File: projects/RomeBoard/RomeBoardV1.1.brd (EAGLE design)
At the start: 120 x 140 mm, 31 parts, among them J1 HEADER-5, J2 RASPBERRY-PI-HEADER, M1 ZVN4424A, M2 ZVN4424A, M3 ZVN4424A, U1 LM1084IT-ADJ

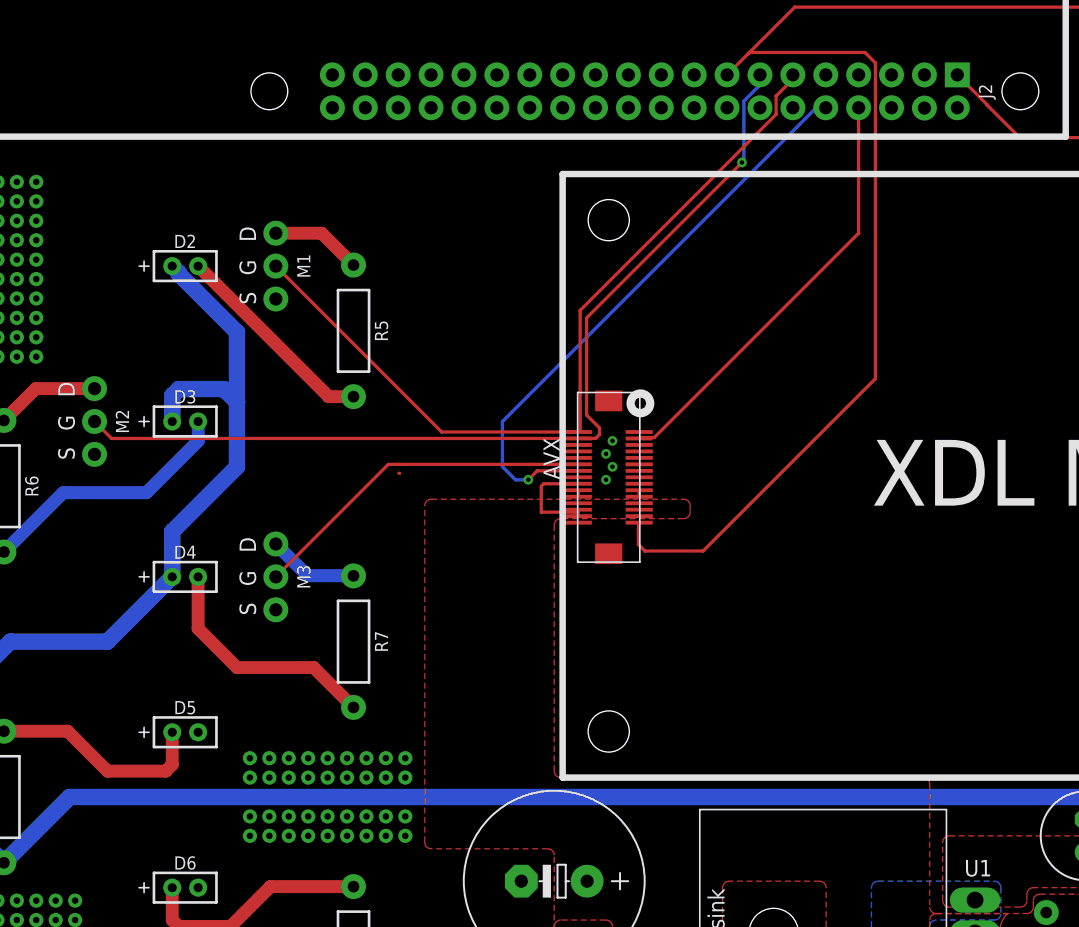
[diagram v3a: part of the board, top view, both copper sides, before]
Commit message: Adding gate pulldowns for NPNs
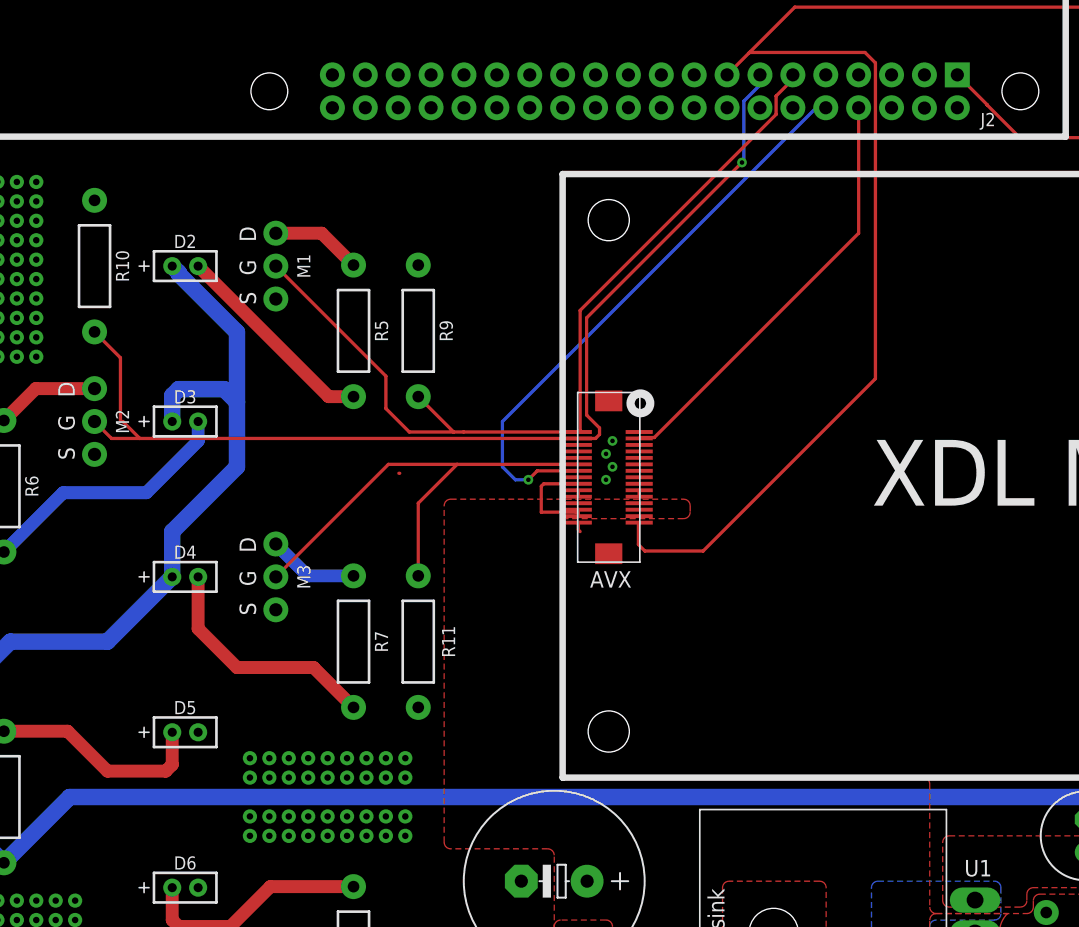
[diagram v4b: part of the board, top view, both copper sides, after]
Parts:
- added R10, R11, R9: 10K, passives:AXIAL-0.4
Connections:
- net GND: now also R10.1, R11.1, R9.1
- net PWR_L: now also R11.2
- net RX_L: now also R10.2
- net TX_L: now also R9.2
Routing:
- net PWR_L: track 27.0 -> 36.8 mm
- net RX_L: track 73.4 -> 83.2 mm
- net TX_L: track 63.1 -> 68.4 mm
- net GND: track 1.07 -> 1.82 mm
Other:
- board text added: "XDL Micro: 435.55MHz"
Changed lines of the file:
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@@
 <hole x="5" y="135" drill="2.844"/>
 <hole x="115" y="135" drill="2.844"/>
-<text x="16" y="133.5" size="3.2" layer="51" font="vector" ratio="19">BROWN SPACE ENGINEERING GROUND STATION</text>
+<text x="17" y="134" size="3.2" layer="51" font="vector" ratio="19">BROWN SPACE ENGINEERING GROUND STATION</text>
 <text x="99.5" y="130.5" size="1.27" layer="51" font="vector" ratio="13">Pi Power</text>
 <text x="106.5" y="103.5" size="2" layer="51" font="vector" ratio="13" align="center">Brown U.
@@
 <text x="16.5" y="11.5" size="1.6764" layer="51" font="vector" ratio="13">3.6V</text>
 <text x="17.5" y="23.5" size="1.6764" layer="51" font="vector" ratio="13">5V</text>
-<text x="107" y="79" size="2.5" layer="51" font="vector" ratio="13" rot="R30" align="center">Che piacere
+<text x="107" y="77.5" size="2.5" layer="51" font="vector" ratio="13" rot="R30" align="center">Che piacere
 vederti!</text>
 <circle x="115" y="135" radius="3.7" width="0.254" layer="20"/>
@@
 <rectangle x1="94.639690625" y1="125.46175" x2="94.784465625" y2="125.51000625" layer="51"/>
 <rectangle x1="94.398390625" y1="125.510009375" x2="94.687946875" y2="125.558265625" layer="51"/>
+<text x="47" y="24" size="1.4224" layer="51" font="vector" ratio="13" rot="R90">XDL Micro: 435.55MHz</text>
 </plain>
 <attributes>
@@
 </autorouter>
 <elements>
-<element name="AVX" library="CNTRL_BOARD" package="AVX-24-5046-630-829" value="AVX-24-5046-030-630-829" x="51.71" y="46.74" rot="R270"/>
+<element name="AVX" library="CNTRL_BOARD" package="AVX-24-5046-630-829" value="AVX-24-5046-030-630-829" x="51.71" y="46.74" smashed="yes" rot="R270">
+<attribute name="NAME" x="50.26" y="38.17" size="1.27" layer="21"/>
+</element>
 <element name="V4" library="BrownSpaceEngineering" package="VIA-120MIL" value="GND" x="14.25" y="4.94" smashed="yes">
 <attribute name="VALUE" x="16.21" y="6.98" size="1.016" layer="27" font="vector" ratio="13"/>
@@
 </element>
 <element name="U$2" library="BrownSpaceEngineering" package="PJ-002A" value="PJ-002A" x="110" y="11" rot="R270"/>
-<element name="J2" library="BrownSpaceEngineering" package="HEADER-20X02" value="RASPBERRY-PI-HEADER" x="54.5" y="76.5" rot="R270"/>
+<element name="J2" library="BrownSpaceEngineering" package="HEADER-20X02" value="RASPBERRY-PI-HEADER" x="54.5" y="76.5" smashed="yes" rot="R270">
+<attribute name="NAME" x="81" y="73.8064" size="1.016" layer="25" font="vector" ratio="20" align="bottom-center"/>
+</element>
 <element name="J1" library="BrownSpaceEngineering" package="HEADER-05" value="HEADER-5" x="103" y="128.5" rot="R180"/>
 <element name="D2" library="BrownSpaceEngineering" package="1X2-POL" value="LEDTHRU-HOLE-CONNECTOR" x="19" y="63" smashed="yes">
@@
 <attribute name="VALUE" x="95.429" y="89.794" size="1.27" layer="27" ratio="10" rot="R180"/>
 </element>
+<element name="R9" library="passives" package="AXIAL-0.4" value="10K" x="37" y="58" rot="R270"/>
+<element name="R10" library="passives" package="AXIAL-0.4" value="10K" x="12" y="63" rot="R270"/>
+<element name="R11" library="passives" package="AXIAL-0.4" value="10K" x="37" y="34" smashed="yes" rot="R90">
+<attribute name="NAME" x="39.849" y="34" size="1.016" layer="25" font="vector" ratio="20" rot="R90" align="bottom-center"/>
+<attribute name="VALUE" x="37.508" y="34" size="1.016" layer="27" font="vector" ratio="20" rot="R90" align="bottom-center"/>
+</element>
 </elements>
 <signals>
@@
 <contactref element="C1" pad="-"/>
 <contactref element="C3" pad="-"/>
-<wire x1="49.36" y1="45.69" x2="49.36" y2="45.19" width="0.254" layer="1"/>
 <via x="52" y="49.5" extent="1-16" drill="0.35"/>
 <via x="51.5" y="48.5" extent="1-16" drill="0.35"/>
@@
 <contactref element="C5" pad="2"/>
 <contactref element="FAN2" pad="2"/>
-<wire x1="49.36" y1="45.19" x2="49.36" y2="43.19" width="0" layer="19" extent="1-1"/>
+<wire x1="49.36" y1="45.19" x2="49.36" y2="45.69" width="0.254" layer="1"/>
+<wire x1="49.36" y1="43.19" x2="49.36" y2="42.64" width="0.254" layer="1"/>
+<wire x1="49.36" y1="42.64" x2="49.5" y2="42.5" width="0.254" layer="1"/>
+<contactref element="R10" pad="1"/>
+<contactref element="R9" pad="1"/>
+<contactref element="R11" pad="1"/>
 </signal>
 <signal name="3V6">
@@
 <vertex x="47.5" y="17.5" curve="90"/>
 <vertex x="47" y="18"/>
-<vertex x="38" y="18" curve="-90"/>
-<vertex x="37.5" y="18.5"/>
-<vertex x="37.5" y="44.5" curve="-90"/>
-<vertex x="38" y="45"/>
+<vertex x="39.5" y="18" curve="-90"/>
+<vertex x="39" y="18.5"/>
+<vertex x="39" y="44.5" curve="-90"/>
+<vertex x="39.5" y="45"/>
 <vertex x="57.5" y="45" curve="-90"/>
 <vertex x="58" y="44.5"/>
 <vertex x="58" y="44" curve="-90"/>
 <vertex x="57.5" y="43.5"/>
-<vertex x="48" y="43.5" curve="90"/>
-<vertex x="47.5" y="43"/>
-<vertex x="47.5" y="24" curve="90"/>
-<vertex x="48" y="23.5"/>
+<vertex x="48.5" y="43.5" curve="90"/>
+<vertex x="48" y="43"/>
+<vertex x="48" y="24" curve="90"/>
+<vertex x="48.5" y="23.5"/>
 <vertex x="76" y="23.5" curve="-90"/>
 <vertex x="76.5" y="23"/>
@@
 <contactref element="J2" pad="P11"/>
 <contactref element="M1" pad="2"/>
-<wire x1="49.36" y1="50.19" x2="38.81" y2="50.19" width="0.254" layer="1"/>
-<wire x1="38.81" y1="50.19" x2="26" y2="63" width="0.254" layer="1"/>
+<wire x1="49.36" y1="50.19" x2="40.5" y2="50.19" width="0.254" layer="1"/>
 <wire x1="49.36" y1="50.19" x2="49.5" y2="50.33" width="0.254" layer="1"/>
 <wire x1="64.6346" y1="74.71446875" x2="64.6346" y2="76.1346" width="0.254" layer="1"/>
@@
 <wire x1="65.93" y1="77.43" x2="65.93" y2="77.77" width="0.254" layer="1"/>
 <wire x1="64.6346" y1="76.1346" x2="65.93" y2="77.43" width="0.254" layer="1"/>
+<contactref element="R9" pad="2"/>
+<wire x1="26" y1="63" x2="34.5" y2="54.5" width="0.254" layer="1"/>
+<wire x1="34.5" y1="54.5" x2="34.5" y2="52" width="0.254" layer="1"/>
+<wire x1="34.5" y1="52" x2="36.31" y2="50.19" width="0.254" layer="1"/>
+<wire x1="36.31" y1="50.19" x2="39.73" y2="50.19" width="0.254" layer="1"/>
+<wire x1="37" y1="52.92" x2="39.73" y2="50.19" width="0.254" layer="1"/>
+<wire x1="39.73" y1="50.19" x2="40.5" y2="50.19" width="0.254" layer="1"/>
 </signal>
 <signal name="RX_L">
@@
 <contactref element="M2" pad="2"/>
 <wire x1="13.31" y1="49.69" x2="12" y2="51" width="0.254" layer="1"/>
-<wire x1="49.36" y1="49.69" x2="13.31" y2="49.69" width="0.254" layer="1"/>
+<wire x1="49.36" y1="49.69" x2="15.5" y2="49.69" width="0.254" layer="1"/>
+<wire x1="15.5" y1="49.69" x2="13.31" y2="49.69" width="0.254" layer="1"/>
 <wire x1="49.36" y1="49.69" x2="50.69" y2="49.69" width="0.254" layer="1"/>
 <wire x1="50.69" y1="49.69" x2="51" y2="50" width="0.254" layer="1"/>
@@
 <wire x1="62" y1="71" x2="62.1454" y2="71.1454" width="0.254" layer="16"/>
 <wire x1="62.1454" y1="71.1454" x2="62.1454" y2="75.74553125" width="0.254" layer="16"/>
+<contactref element="R10" pad="2"/>
+<wire x1="15.5" y1="49.69" x2="14.19" y2="51" width="0.254" layer="1"/>
+<wire x1="14.19" y1="51" x2="14" y2="51" width="0.254" layer="1"/>
+<wire x1="14" y1="55.92" x2="12" y2="57.92" width="0.254" layer="1"/>
+<wire x1="14" y1="51" x2="14" y2="55.92" width="0.254" layer="1"/>
 </signal>
 <signal name="PWR_L">
 <contactref element="AVX" pad="P12"/>
 <contactref element="M3" pad="2"/>
-<wire x1="49.36" y1="47.69" x2="34.69" y2="47.69" width="0.254" layer="1"/>
+<wire x1="49.36" y1="47.69" x2="40" y2="47.69" width="0.254" layer="1"/>
+<wire x1="40" y1="47.69" x2="34.69" y2="47.69" width="0.254" layer="1"/>
 <wire x1="34.69" y1="47.69" x2="26" y2="39" width="0.254" layer="1"/>
+<contactref element="R11" pad="2"/>
+<wire x1="40" y1="47.69" x2="37" y2="44.69" width="0.254" layer="1"/>
+<wire x1="37" y1="44.69" x2="37" y2="39.08" width="0.254" layer="1"/>
 </signal>
 <signal name="N$2">

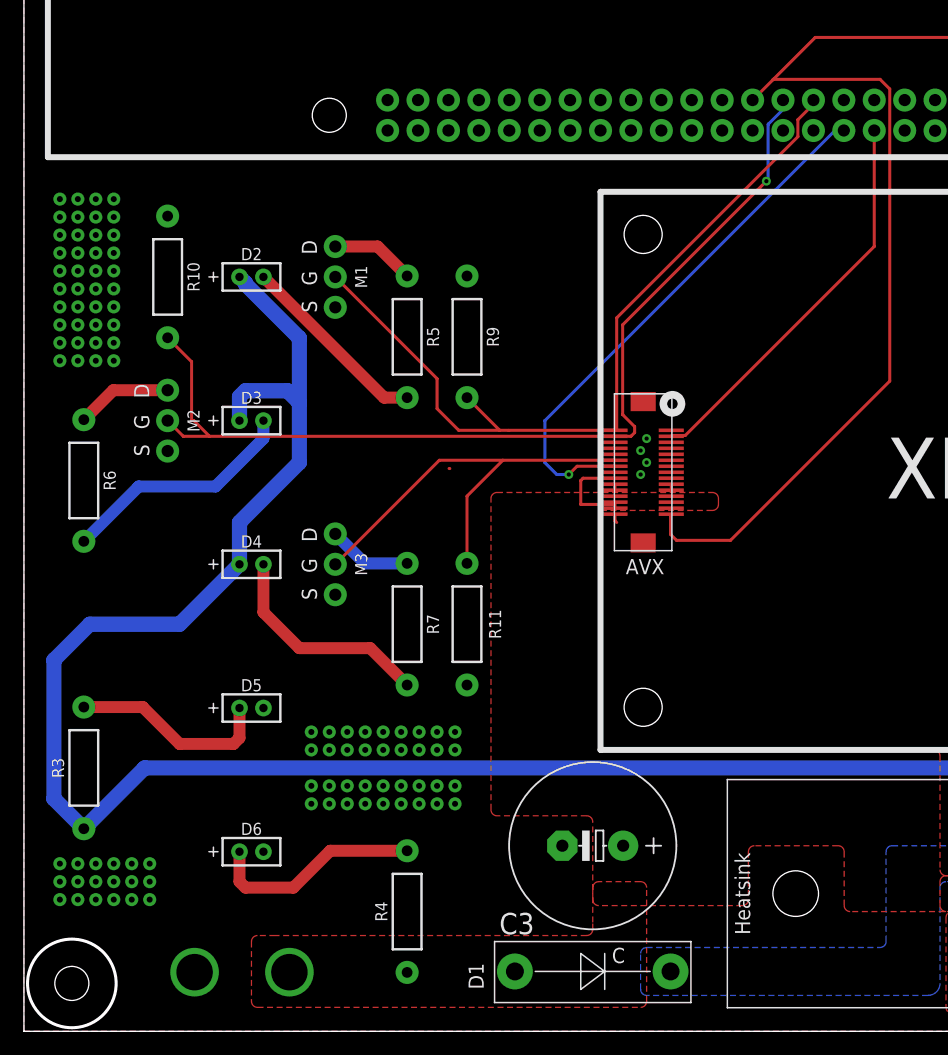
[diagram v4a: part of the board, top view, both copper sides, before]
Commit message: adding vias and moving silkscreen around a bit
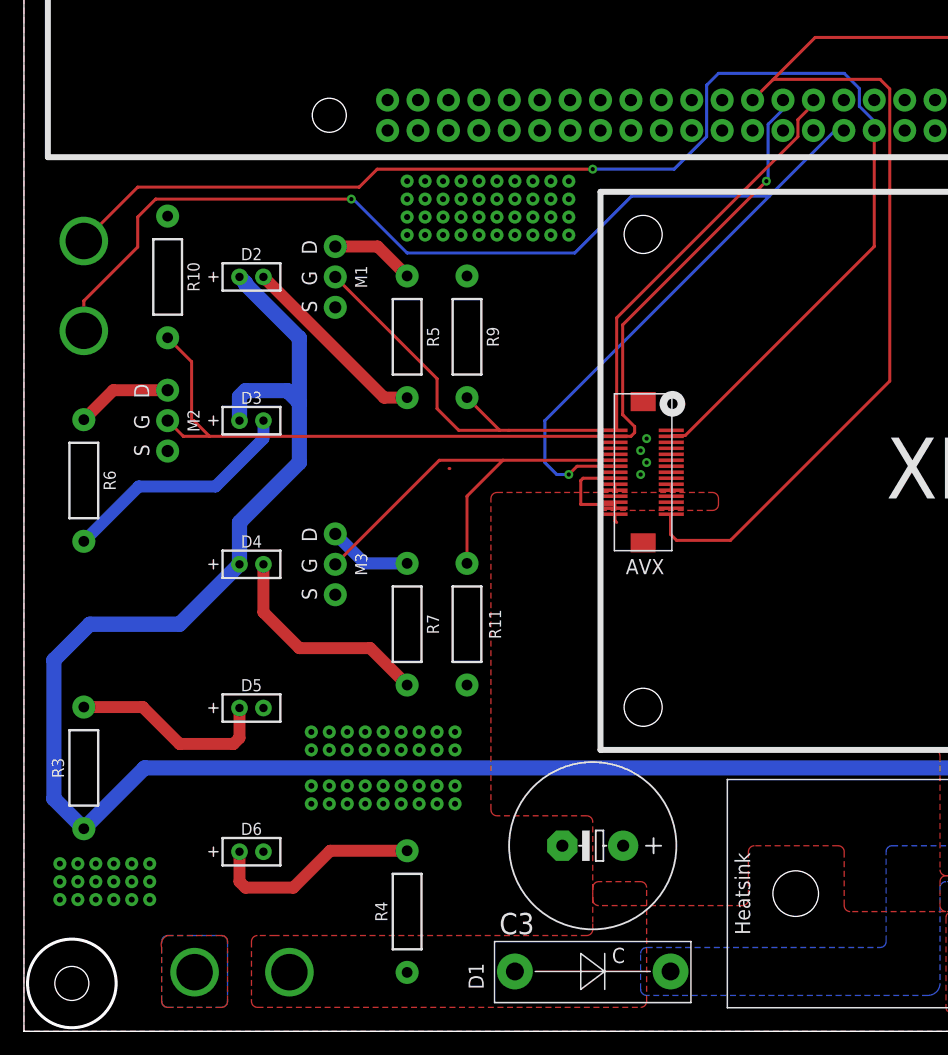
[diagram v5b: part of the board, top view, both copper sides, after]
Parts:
- added V1: TX_D, BrownSpaceEngineering:VIA-120MIL
- added V2: RX_D, BrownSpaceEngineering:VIA-120MIL
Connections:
- net RX_D: now also V2.P$1
- net TX_D: now also V1.P$1
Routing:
- net TX_D: track 33.2 -> 110.8 mm, vias 0 -> 1
- net RX_D: track 45.1 -> 113.6 mm, vias 1 -> 2
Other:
- board text added: "Raspberry Pi 3 Model B"
- board text added: "Viviana Arrunategui Mckenna Cisler Tyler Fox Manav Kohli Caelan Ritter"
- board text removed: "Viviana Arrunategui Manav Kohli Caelan Ritter"

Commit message: final version of 1.1B (pending very minor changes)
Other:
- outline, holes or cut-outs redrawn
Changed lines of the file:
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@@
 <layer number="46" name="Milling" color="3" fill="1" visible="no" active="yes"/>
 <layer number="47" name="Measures" color="7" fill="1" visible="no" active="yes"/>
-<layer number="48" name="Document" color="7" fill="1" visible="yes" active="yes"/>
+<layer number="48" name="Document" color="7" fill="1" visible="no" active="yes"/>
 <layer number="49" name="Reference" color="7" fill="1" visible="no" active="yes"/>
 <layer number="50" name="dxf" color="7" fill="1" visible="no" active="no"/>
@@
 <wire x1="118" y1="23.5" x2="118" y2="70.11" width="0.5" layer="21"/>
 <text x="72" y="44.5" size="5.08" layer="21" font="vector" ratio="13">XDL Micro</text>
-<hole x="4" y="4" drill="2.844"/>
+<hole x="5" y="5" drill="2.844"/>
 <hole x="115" y="5" drill="2.844"/>
 <hole x="5" y="135" drill="2.844"/>
@@
 <circle x="5" y="135" radius="3.7" width="0.254" layer="20"/>
 <circle x="115" y="5" radius="3.7" width="0.254" layer="20"/>
-<circle x="4" y="4" radius="3.7" width="0.254" layer="20"/>
+<circle x="5" y="5" radius="3.7" width="0.254" layer="20"/>
 <text x="109.5" y="16" size="2.1844" layer="51" font="vector" ratio="13">5V in</text>
 <rectangle x1="94.398390625" y1="114.072390625" x2="94.687946875" y2="114.120646875" layer="51"/>
@@
 <rectangle x1="94.639690625" y1="125.46175" x2="94.784465625" y2="125.51000625" layer="51"/>
 <rectangle x1="94.398390625" y1="125.510009375" x2="94.687946875" y2="125.558265625" layer="51"/>
-<text x="47" y="24" size="1.4224" layer="51" font="vector" ratio="13" rot="R90">XDL Micro: 435.55MHz</text>
-<text x="2" y="71" size="1.4224" layer="48" font="vector" ratio="13">Raspberry Pi 3 Model B</text>
+<text x="47.5" y="24" size="1.4224" layer="51" font="vector" ratio="13" rot="R90">XDL Micro: 435.55MHz</text>
+<text x="2" y="71" size="1.4224" layer="51" font="vector" ratio="13">Raspberry Pi 3 Model B</text>
 </plain>
 <attributes>
